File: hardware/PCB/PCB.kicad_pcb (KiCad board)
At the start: 2 copper layers, 30.4 x 52.6 mm, 42 parts, among them J1 Conn_01x02_Pin, J2 USB_C_Receptacle_USB2.0_14P, J3 Conn_01x04_Pin, Q1 BC807, Q2 BC817, Q3 BC817, SW1 SW_Push, SW2 SW_Push, U1 ESP32-C6-MINI-1, U2 AP3015, U3 MCP1700x-330xxTT

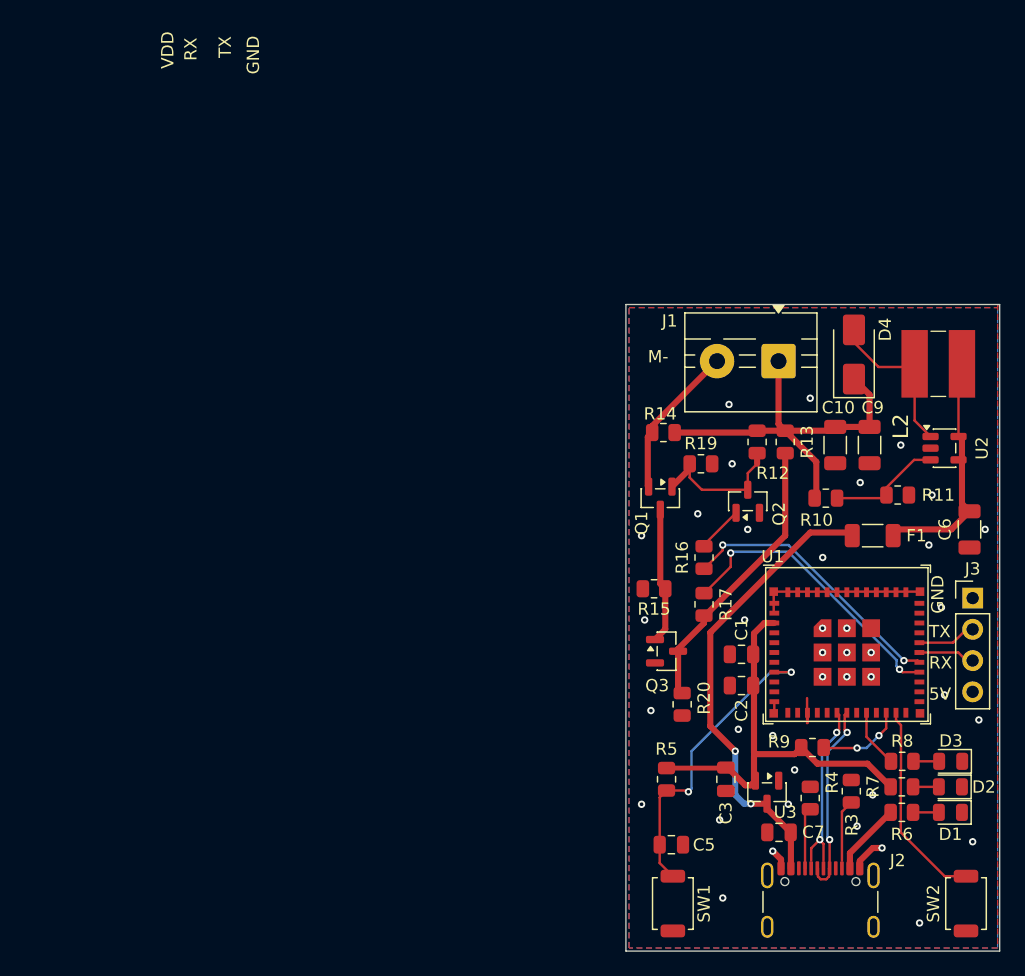
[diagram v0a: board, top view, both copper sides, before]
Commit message: Revision F appears done.
I moved the capacitors and inductor positions.
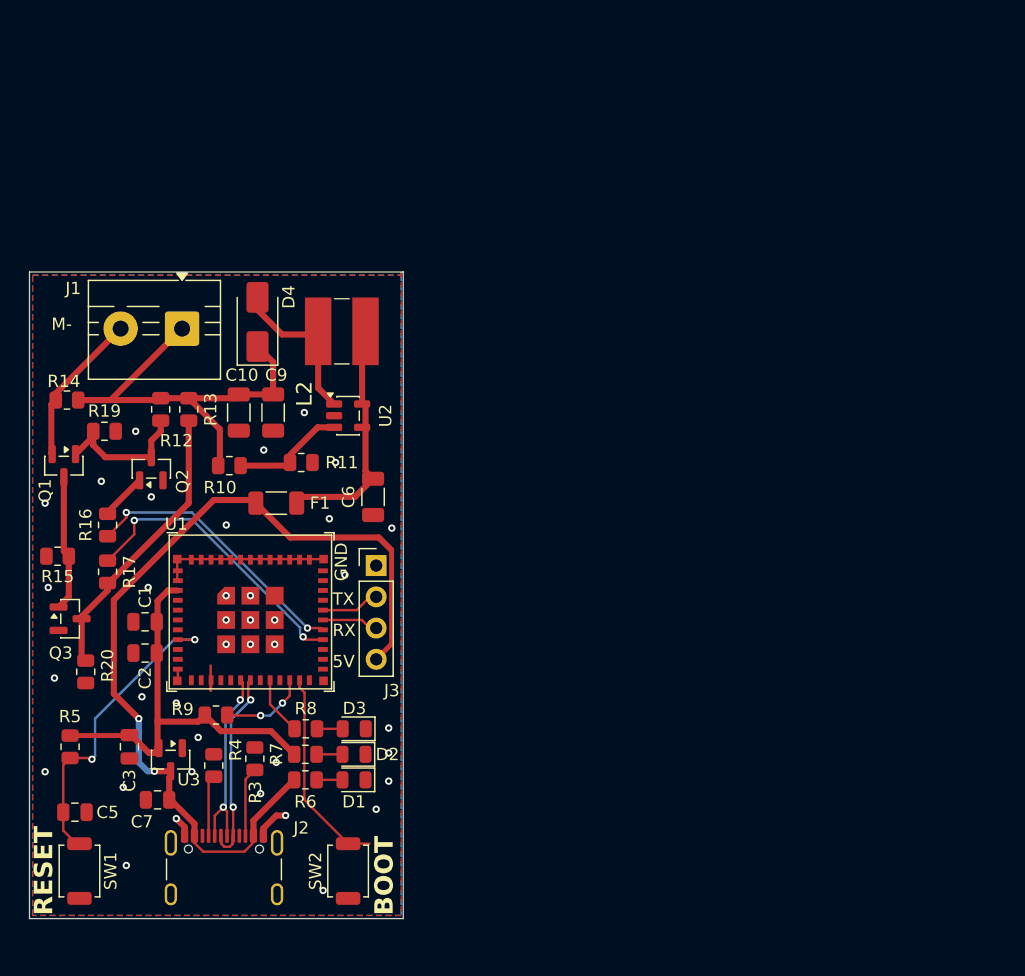
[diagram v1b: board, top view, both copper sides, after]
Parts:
- moved C7 50.6 mm to (92.5, 77.9)
- moved SW2 50.3 mm to (108.0, 83.7)
- moved C10 48.6 mm to (99.1, 46.4)
- moved D4 48.6 mm to (100.6, 39.0)
- moved F1 48.6 mm to (102.1, 53.7)
- moved R14 48.6 mm to (85.1, 45.4)
- moved R15 48.6 mm to (84.3, 58.1)
- moved R9 48.6 mm to (97.2, 71.0)
- moved C1 48.6 mm to (91.5, 63.4)
- moved C2 48.6 mm to (91.5, 65.9)
- moved C5 48.6 mm to (85.7, 78.9)
- moved C6 48.6 mm to (110.0, 53.2)
- moved D3 48.6 mm to (108.5, 72.1)
- moved J1 48.6 mm to (94.5, 39.6)
- moved J2 48.6 mm to (97.9, 84.5)
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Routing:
- net +5V: track 43.8 -> 72.6 mm
- net MBUS+: track 32.9 -> 37.9 mm
- net GND: vias 39 -> 38
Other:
- board text added: "BOOT"
- board text added: "RESET"
- board text removed: "VDD"

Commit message: Another few tweaks to tighten voltage booster components. Swapped debug header to remove long 5V trace
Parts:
- moved J3 7.72 mm to (110.2, 66.5), turned to 180 degrees
- moved C6 3.45 mm to (110.0, 49.8)
- moved U2 1.17 mm to (108.0, 45.5)
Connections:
- J3 pad 2: UART0_TX -> UART0_RX
- J3 pad 3: UART0_RX -> UART0_TX
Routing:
- net +5V: track 72.6 -> 62.6 mm
- net BOOT: track 16.7 -> 14.9 mm
- net Net-(D4-A): track 12.2 -> 11.1 mm
- net Net-(U2-IN): track 18.9 -> 17.8 mm
- net GND: vias 38 -> 37

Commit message: More tweaks to revision F
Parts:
- moved R10 7.47 mm to (103.9, 45.7), turned to -90 degrees
- moved U2 1.00 mm to (109.0, 45.5)
- moved D4 1.00 mm to (101.1, 39.9)
- moved R3 0.91 mm to (100.4, 75.4)
- moved C10 0.53 mm to (98.6, 46.5)
- moved C9 0.52 mm to (101.3, 46.4)
- moved R15 0.50 mm to (84.8, 58.1)
- moved C5 0.39 mm to (85.7, 78.5)
- moved R4 0.36 mm to (97.0, 75.4)
- moved SW1 0.35 mm to (86.1, 83.3)
- moved SW2 0.35 mm to (108.0, 83.3)
- moved R14 0.27 mm to (84.8, 45.4)
- moved R20 0.27 mm to (86.4, 67.5)
- moved Q2 0.10 mm to (92.0, 51.1)
- moved R11 0.10 mm to (104.2, 50.5), turned to 180 degrees
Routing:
- net MBUS+: track 37.9 -> 34.2 mm
- net Net-(U2-FB): track 9.73 -> 8.43 mm
- net Net-(D4-A): track 11.1 -> 12.1 mm
- net GND: track 22.2 -> 23.1 mm
- net Net-(J2-CC2): track 5.04 -> 4.13 mm
- net UART1_RX: track 24.0 -> 23.5 mm
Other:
- board text added: "M+"
- board text added: "Tomás McGuinness MBus-ESP32 Revision: ${REVISION}"
- board text removed: "Tomas McGuinness MBus-ESP32 Revision: ${REVISION}"
